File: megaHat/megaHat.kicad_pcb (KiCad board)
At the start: 2 copper layers, 101.6 x 53.3 mm, 40 parts, among them J1 +7.6V GND, J2 Conn_EMG, J3 Conn _CV, M1 Motor_Servo, M2 Motor_Servo, M3 Motor_Servo, M4 Motor_Servo, SW1 Reset, SW2 PushButton, U1 PCA9548ADB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

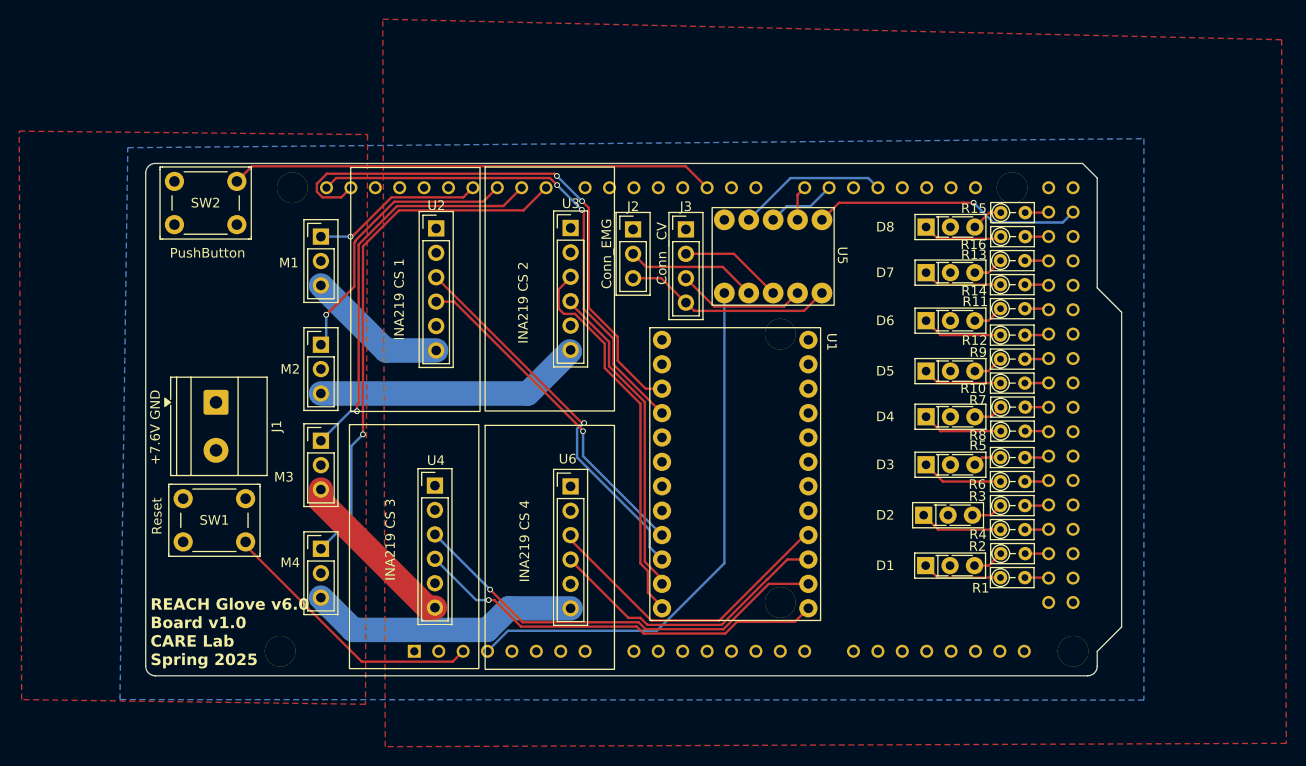
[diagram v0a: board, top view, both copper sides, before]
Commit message: Vias large, added images for fab
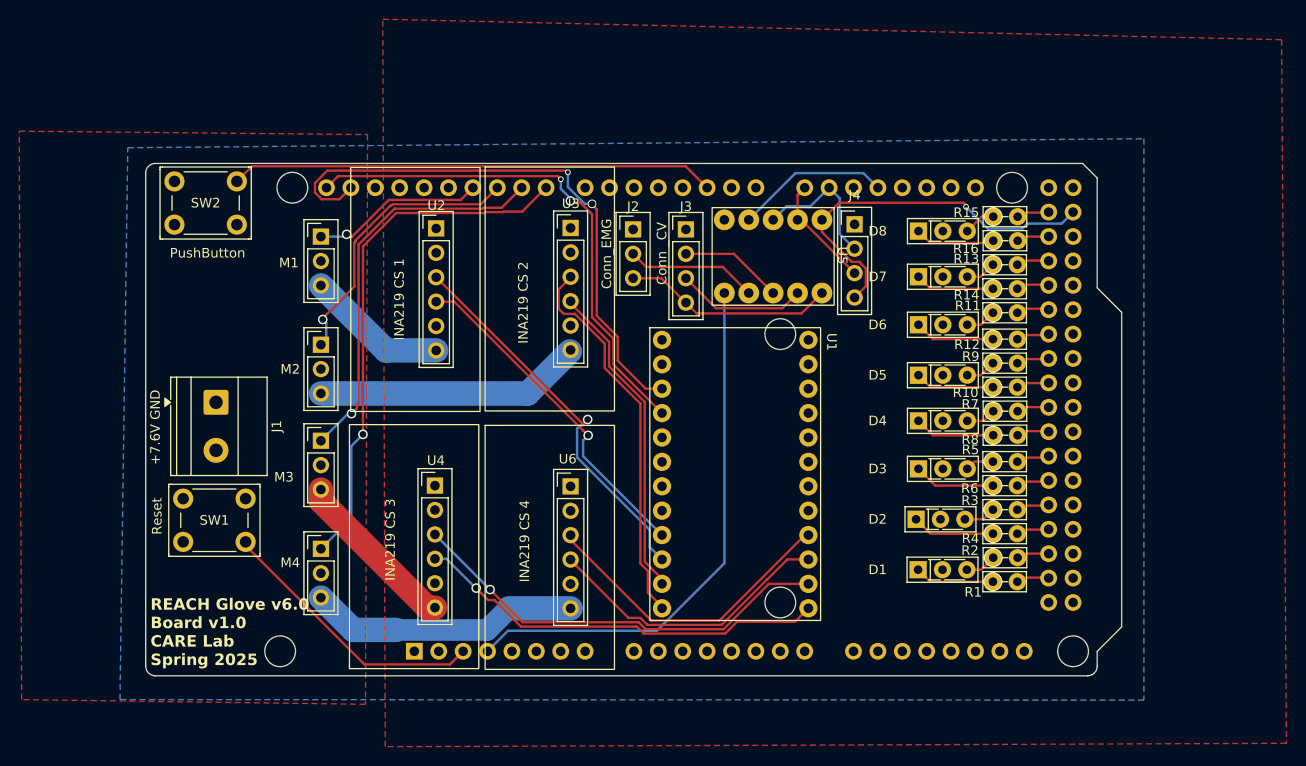
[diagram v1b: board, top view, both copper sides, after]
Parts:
- added J4: Conn _CV-5V, Connector_PinHeader_2.54mm:PinHeader_1x04_P2.54mm_Vertical, F.Cu at (154.6, 60.0)
- moved D1 0.90 mm to (161.2, 95.9)
- moved D2 0.90 mm to (161.0, 90.7)
- moved D3 0.90 mm to (161.2, 85.4)
- moved D4 0.90 mm to (161.2, 80.4)
- moved D5 0.90 mm to (161.2, 75.7)
- moved D6 0.90 mm to (161.2, 70.4)
- moved D7 0.90 mm to (161.2, 65.4)
- moved D8 0.90 mm to (161.2, 60.7)
- moved R1 0.90 mm to (169.0, 97.2)
- moved R10 0.90 mm to (169.0, 76.9)
- moved R11 0.90 mm to (169.0, 69.2)
- moved R12 0.90 mm to (169.0, 71.9)
- moved R13 0.90 mm to (169.0, 64.2)
- moved R14 0.90 mm to (169.0, 66.7)
- moved R15 0.90 mm to (169.0, 59.2)
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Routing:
- net /D23: track 28.2 -> 39.8 mm
- net /TX3: track 3.65 -> 11.9 mm
- net /RX3: track 7.21 -> 14.7 mm
- net /SDA: track 58.7 -> 61.0 mm
- net /SCL: track 53.5 -> 54.7 mm
- net Net-(U1-SC0): track 40.0 -> 41.0 mm
